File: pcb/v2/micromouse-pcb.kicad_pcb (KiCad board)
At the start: 2 copper layers, 120 x 80 mm, 49 parts, among them J1_MotorEncoder1 Conn_01x06, J2_MotorEncoder1 Conn_01x06, J3 Conn_01x08, J4 Conn_01x08, Q1 BS170, Q2 TEFT4300, Q3 BS170, Q4 TEFT4300, Q5 BS170, Q6 TEFT4300, Q7 BS170, Q8 TEFT4300, SW1 SW_SPDT, U0 Teensy 4.1, U2 L7805

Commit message: Got gyro in
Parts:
- added J1: Conn_01x08, Connector_PinSocket_2.54mm:PinSocket_1x08_P2.54mm_Vertical, F.Cu at (40.5, 46.4)
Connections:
- U0 pad 16: Signal M2_A -> unconnected-(U0-A2-Pad16)
- U0 pad 17: Signal M2_B -> unconnected-(U0-A3-Pad17)
- U0 pad 18: PWM M1_A -> SDA
- U0 pad 19: PWM M1_B -> SCL
- U0 pad 28: unconnected-(U0-RX7-Pad28) -> PWM M1_A
- U0 pad 29: unconnected-(U0-TX7-Pad29) -> PWM M1_B
- U0 pad 40: unconnected-(U0-A16-Pad40) -> Signal M2_A
- U0 pad 41: unconnected-(U0-A17-Pad41) -> Signal M2_B
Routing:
- net SCL: track 0.00 -> 17.0 mm
- net SDA: track 0.00 -> 17.0 mm
- net 3.3V: track 251.1 -> 267.6 mm, vias 1 -> 2
- net PWM M1_A: track 56.4 -> 71.1 mm
- net PWM M1_B: track 61.7 -> 67.4 mm
- net Signal M2_B: track 55.7 -> 51.6 mm
- net Signal M2_A: track 55.7 -> 51.6 mm
- net Signal M1_A: track 73.2 -> 74.0 mm
- net Receiver 4: track 85.4 -> 86.2 mm

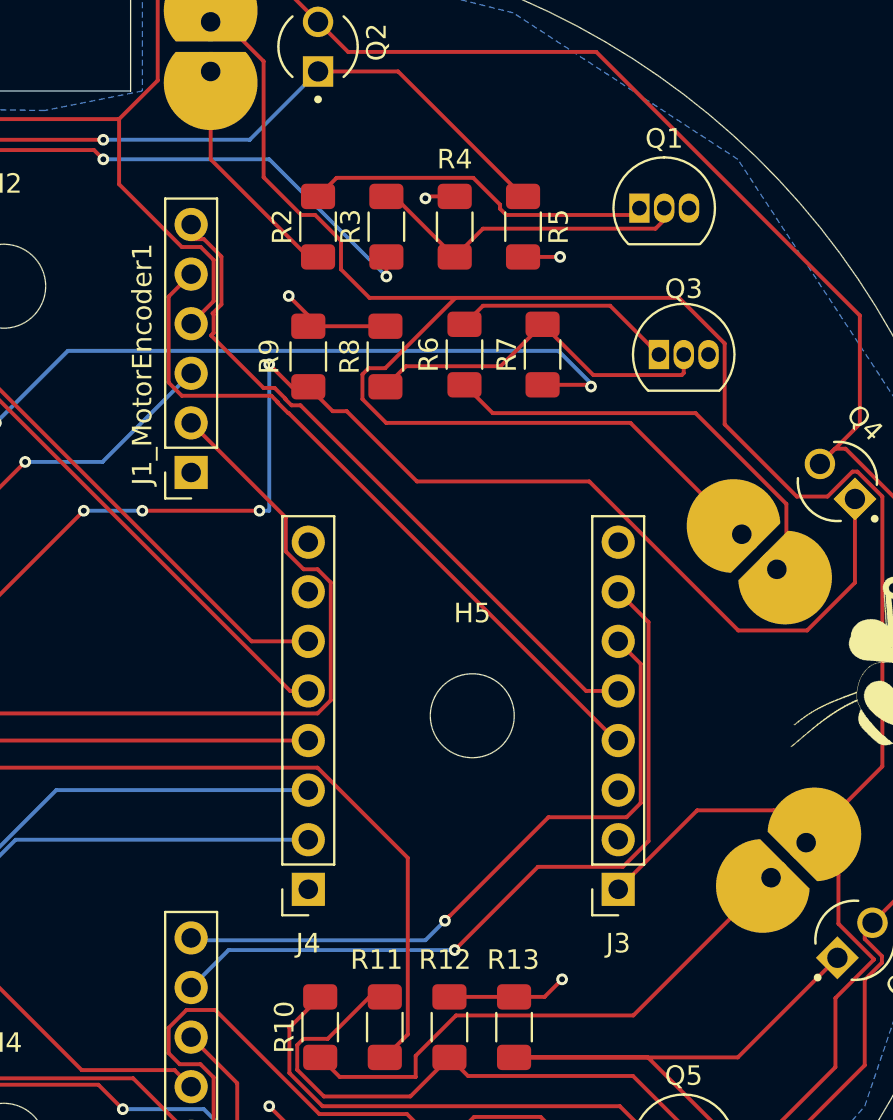
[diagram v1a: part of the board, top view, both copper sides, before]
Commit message: made motor to H-bridge wires wider
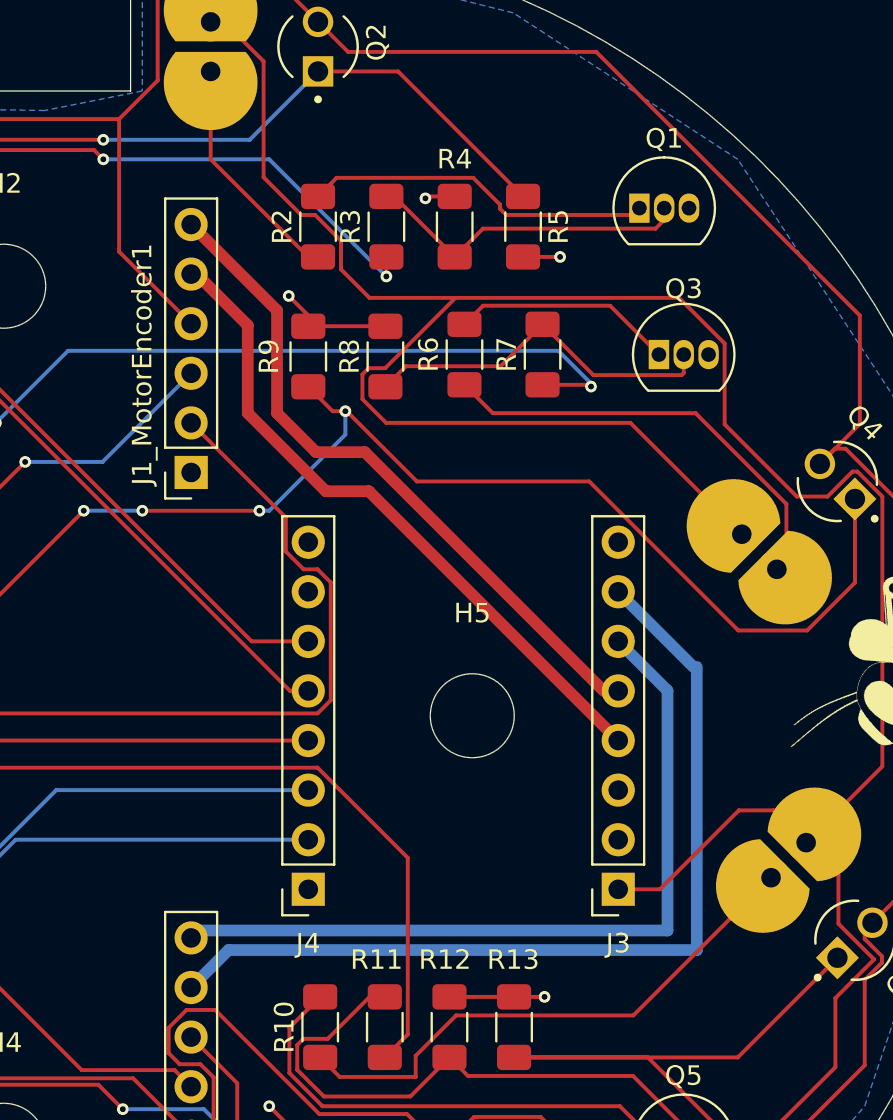
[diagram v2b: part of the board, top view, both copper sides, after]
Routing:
- net M2_A: track 39.9 -> 46.8 mm, vias 1 -> 0
- net M2_B: track 35.1 -> 40.4 mm, vias 1 -> 0
- net Receiver 2: track 128.1 -> 124.9 mm
- net M1_A: track 36.7 -> 34.5 mm
- net 3.3V: track 267.6 -> 266.1 mm
- net GND: track 22.3 -> 21.0 mm

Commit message: Slight changes to schematic
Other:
- copper layers 2 -> 4
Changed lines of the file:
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@@
 	(layers
 		(0 "F.Cu" signal)
+		(4 "In1.Cu" signal)
+		(6 "In2.Cu" signal)
 		(2 "B.Cu" signal)
 		(9 "F.Adhes" user "F.Adhesive")
@@
 			)
 			(layer "dielectric 1"
+				(type "prepreg")
+				(thickness 0.1)
+				(material "FR4")
+				(epsilon_r 4.5)
+				(loss_tangent 0.02)
+			)
+			(layer "In1.Cu"
+				(type "copper")
+				(thickness 0.035)
+			)
+			(layer "dielectric 2"
 				(type "core")
-				(thickness 1.51)
+				(thickness 1.24)
+				(material "FR4")
+				(epsilon_r 4.5)
+				(loss_tangent 0.02)
+			)
+			(layer "In2.Cu"
+				(type "copper")
+				(thickness 0.035)
+			)
+			(layer "dielectric 3"
+				(type "prepreg")
+				(thickness 0.1)
 				(material "FR4")
 				(epsilon_r 4.5)
@@
 		(stroke
 			(width 0.1)
-			(type default)
-		)
-		(layer "Cmts.User")
-	)
-	(gr_line
-		(start 150 40)
-		(end 150 50)
-		(stroke
-			(width 0.1)
